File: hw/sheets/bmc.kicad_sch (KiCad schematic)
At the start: 12 parts, among them SW1 SSSS711403, U10 TS5A3166, U11 DIP-8 Socket, U12 TPS2053BDR, U8 ESP32-S3-WROOM-1-N16R2, U9 TS5A3166

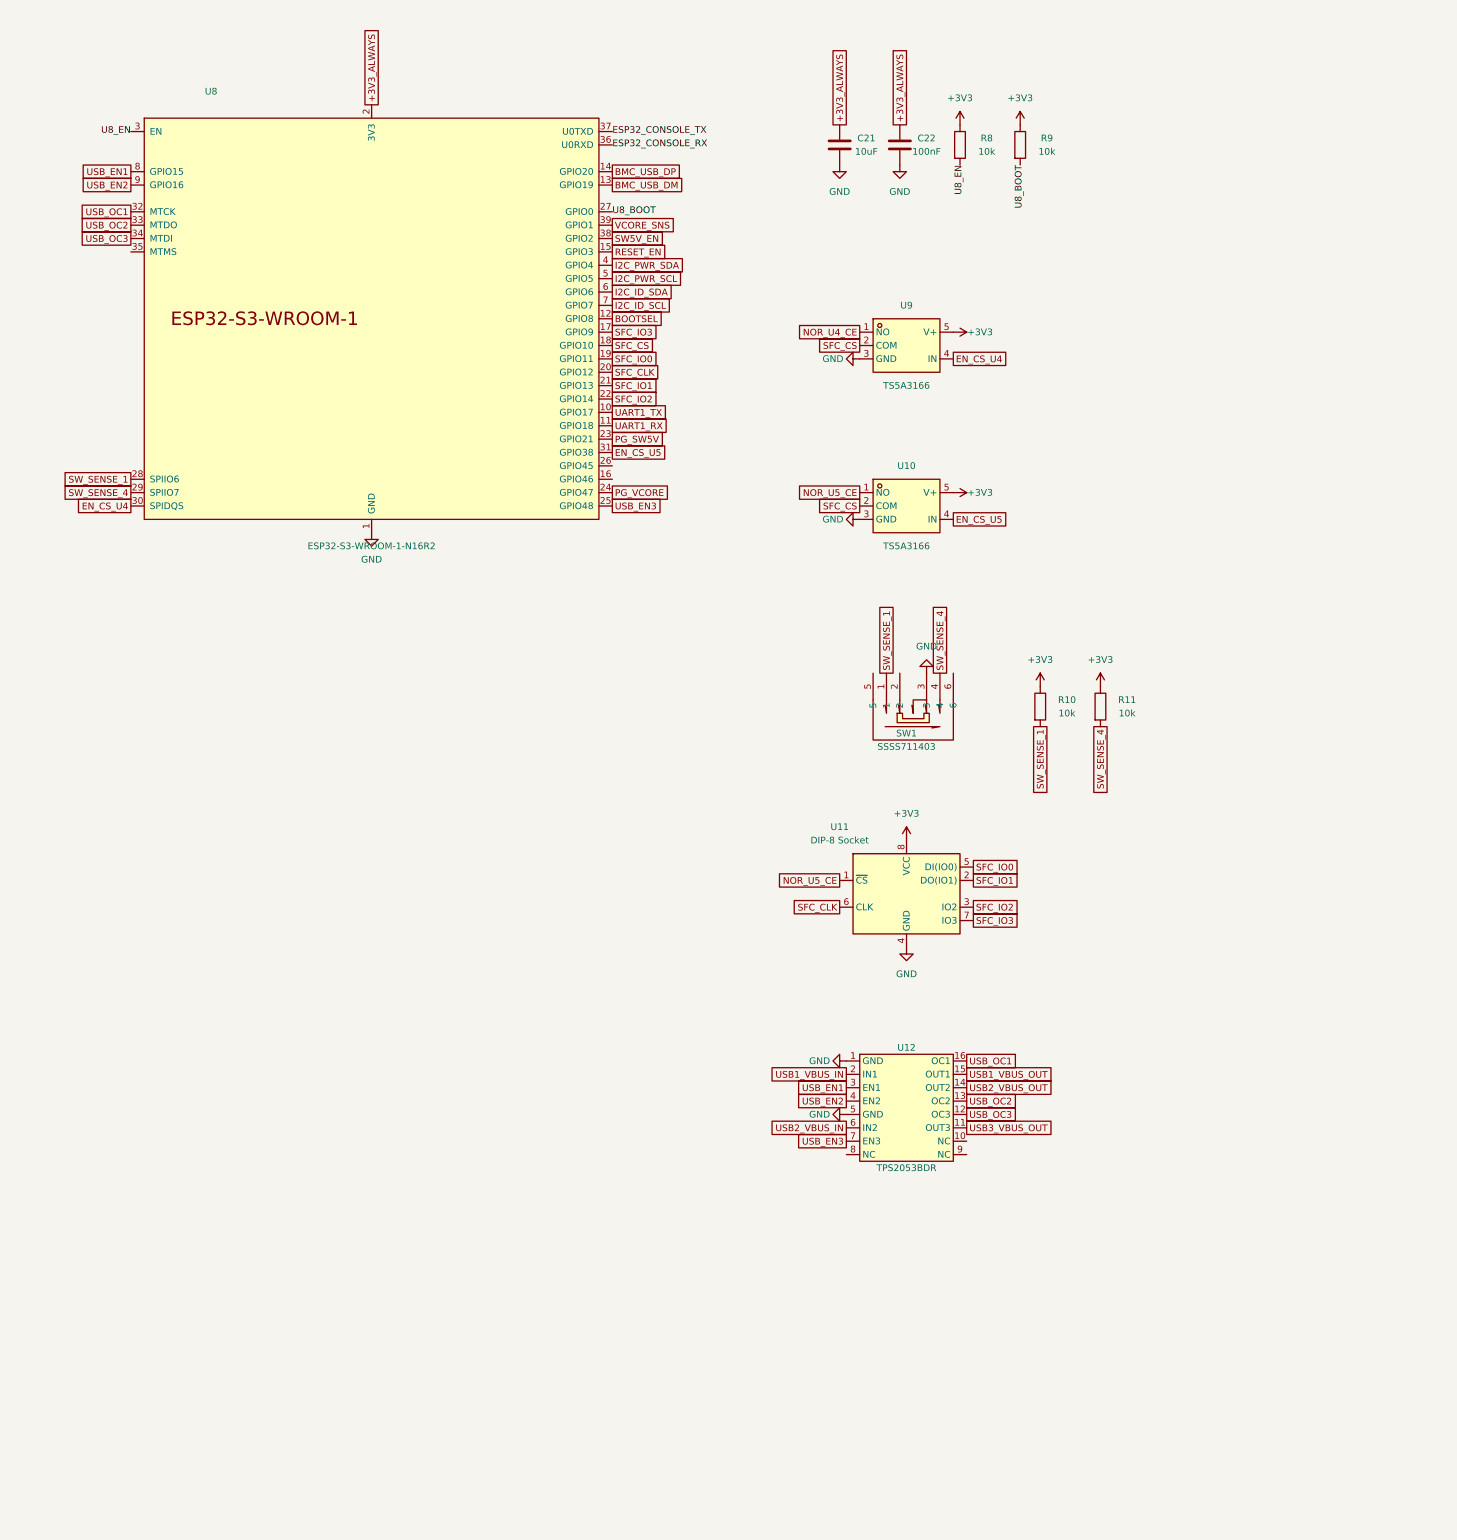
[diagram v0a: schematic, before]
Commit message: Carrier board: BMC power isolation, ESP-Hosted link, GPIO expander
Rebuilds the schematic to connectivity-by-label per BUILD.md (zero
wires/junctions) across all four sections, and adds the BMC power
architecture, connector crossings, and safety fixes worked out this
session:

- Dedicated BMC USB-C (J9), isolated 5V domains (+5V_BMC/+5V_ALT/+5V_SW),
  priority DC-jack-over-USB-C P-FET OR (Q1/Q2), 2:1 load-switch select
  (U4/U14) with a genuine ON-OFF-ON manual override (SW2)
- D1/D2 diode-OR so the BMC stays powered on ALT-only input without
  reopening the J9 backfeed path
- JP1 provisioning jumper + mandatory bring-up checklist: gates SW2 until
  the digipot's NV memory has been confirmed safe, closing the
  factory-mid-scale-default overvoltage gap on VCORE
- GPIO expander (U15, TCA9555PWR) frees 9 ESP32 GPIOs for a full-duplex
  SPI link to the interposer SoC (ESP-Hosted WiFi/BLE co-processor),
  while keeping flash chip-select and power-domain switching native for
  margin testing
- microSD, headphone jack, and both MIPI camera FFCs now cross the DDR4
  connector to the interposer, with GND isolation around each block
- J2/J3 share one USB host data pair to the interposer (peripheral use,
  independent of J2's power role)
- Added missing primary SOIC-8 NOR flash chip (W25Q32JVSS) to match the
  reference board's dual-NOR layout

docs/UNIVERSAL.md updated throughout to match; CONNECTIONS.txt and the
ESP32 pinout reference regenerated from the current netlist.
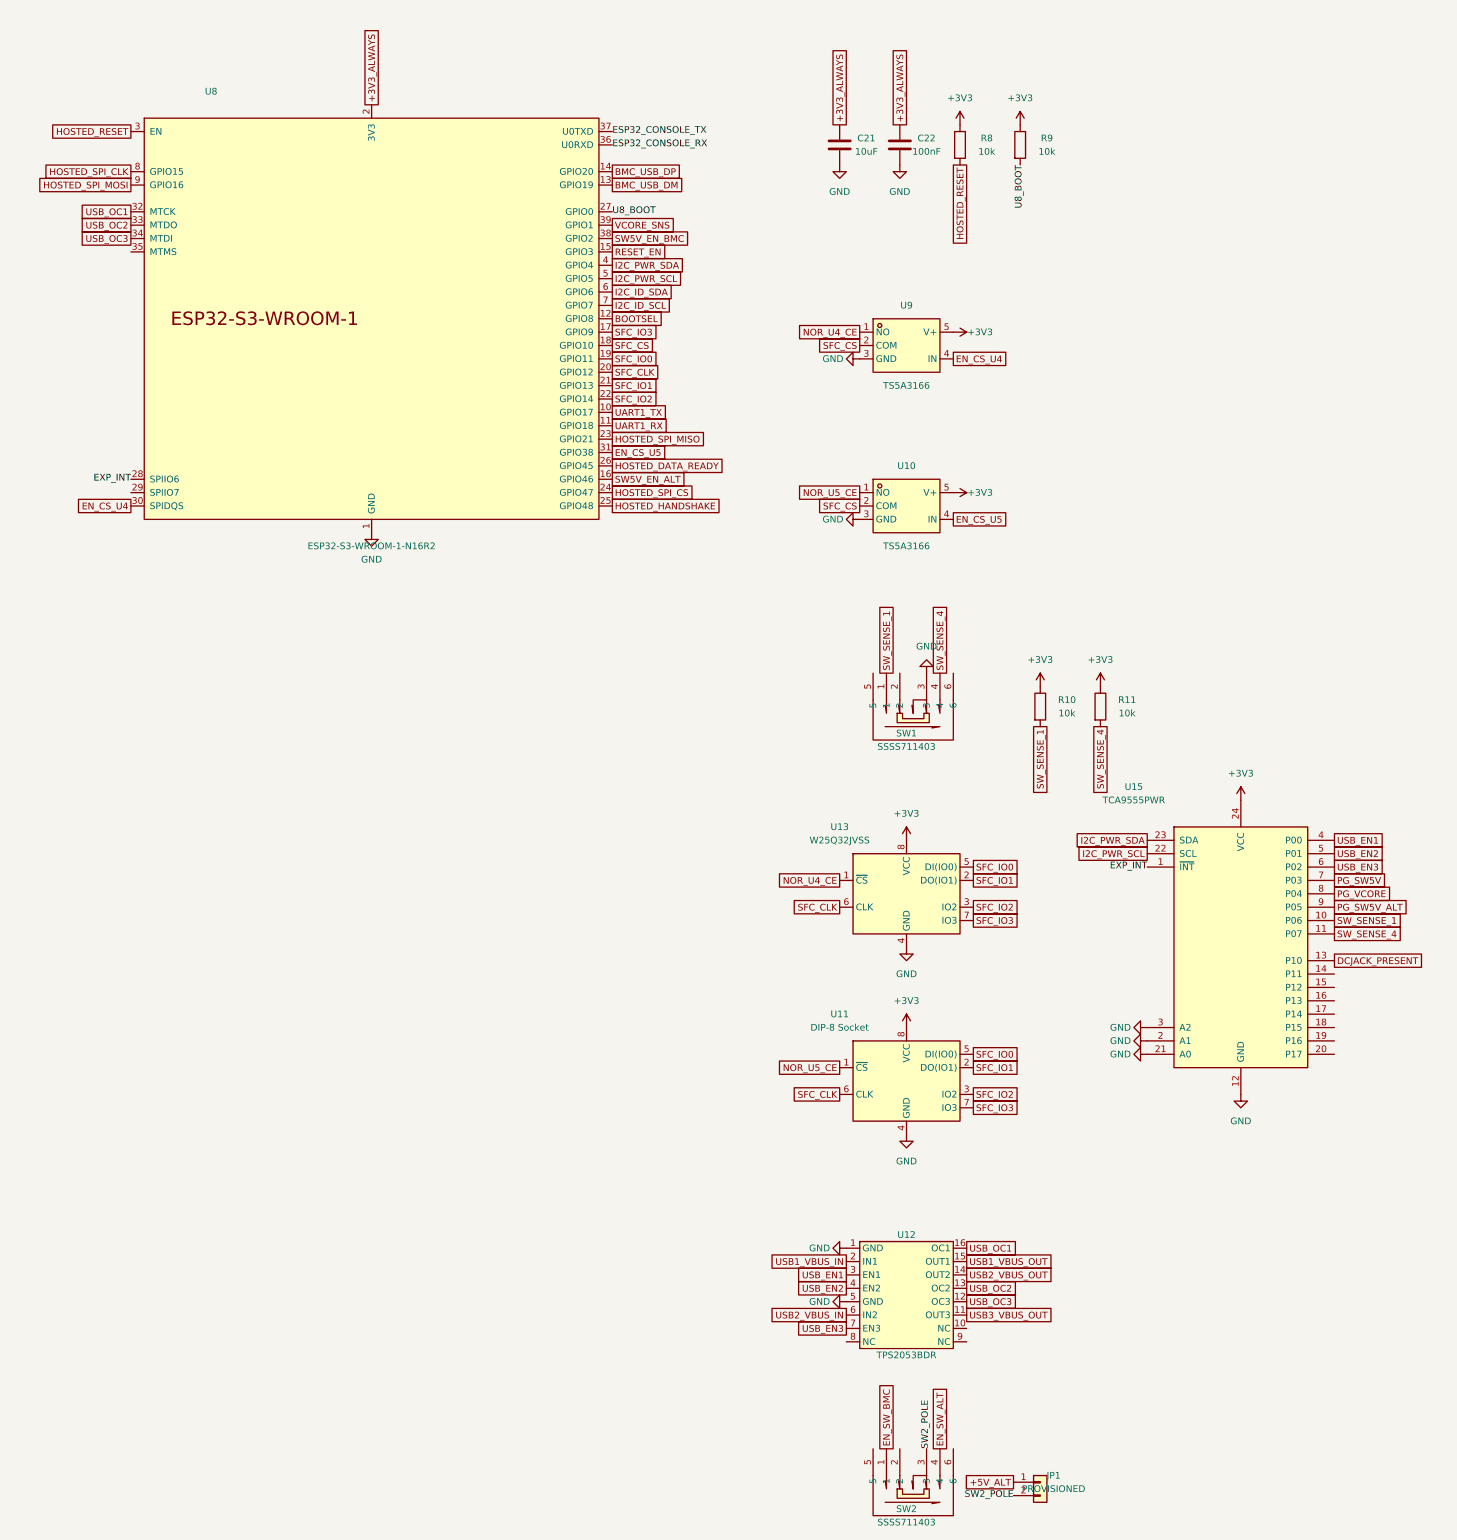
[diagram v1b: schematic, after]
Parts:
- added JP1: PROVISIONED, Connector_PinHeader_2.54mm:PinHeader_1x02_P2.54mm_Vertical, symbol Connector_Generic:Conn_01x02
- added SW2: SSSS711403, teacup-carrier:SW-TH_SSSS711403, symbol teacup-carrier:SSSS711403
- added U13: W25Q32JVSS, Package_SO:SOIC-8_5.23x5.23mm_P1.27mm, symbol teacup-carrier:W25Q32JVSS
- added U15: TCA9555PWR, Package_SO:TSSOP-24_4.4x7.8mm_P0.65mm, symbol teacup-carrier:TCA9555PWR
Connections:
- net +3V3: now also U13.8 (VCC), U15.24 (VCC)
- net GND: now also U13.4 (GND), U15.12 (GND), U15.2 (A1), U15.21 (A0), U15.3 (A2)
- net I2C_PWR_SCL: now also U15.22 (SCL)
- net I2C_PWR_SDA: now also U15.23 (SDA)
- net NOR_U4_CE: now also U13.1 (~{CS})
- net PG_SW5V: now also U15.7 (P03); no longer U8.23 (GPIO21)
- net PG_VCORE: now also U15.8 (P04); no longer U8.24 (GPIO47)
- net SFC_CLK: now also U13.6 (CLK)
- net SFC_IO0: now also U13.5 (DI(IO0))
- net SFC_IO1: now also U13.2 (DO(IO1))
- net SFC_IO2: now also U13.3 (IO2)
- net SFC_IO3: now also U13.7 (IO3)
- net SW_SENSE_1: now also U15.10 (P06); no longer U8.28 (SPIIO6)
- net SW_SENSE_4: now also U15.11 (P07); no longer U8.29 (SPIIO7)
- net USB_EN1: now also U15.4 (P00); no longer U8.8 (GPIO15)
- net USB_EN2: now also U15.5 (P01); no longer U8.9 (GPIO16)
- net USB_EN3: now also U15.6 (P02); no longer U8.25 (GPIO48)
- net SW5V_EN_ALT: now reaches U8.16 (GPIO46)
- net HOSTED_DATA_READY: now reaches U8.26 (GPIO45)
- net SW5V_EN renamed SW5V_EN_BMC
- net U8_EN renamed HOSTED_RESET
- new net +5V_ALT: JP1.1 (Pin_1)
- new net DCJACK_PRESENT: U15.13 (P10)
- new net EN_SW_ALT: SW2.4
- new net EN_SW_BMC: SW2.1
- new net EXP_INT: U15.1 (~{INT}), U8.28 (SPIIO6)
- new net HOSTED_HANDSHAKE: U8.25 (GPIO48)
- new net HOSTED_SPI_CLK: U8.8 (GPIO15)
- new net HOSTED_SPI_CS: U8.24 (GPIO47)
- new net HOSTED_SPI_MISO: U8.23 (GPIO21)
- new net HOSTED_SPI_MOSI: U8.9 (GPIO16)
- new net PG_SW5V_ALT: U15.9 (P05)
- new net SW2_POLE: JP1.2 (Pin_2), SW2.3
